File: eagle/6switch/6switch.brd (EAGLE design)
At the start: 100 x 80 mm, 13 parts, among them IC1 MCP23017SP, J1 RELAYBRD, Q1 BC548

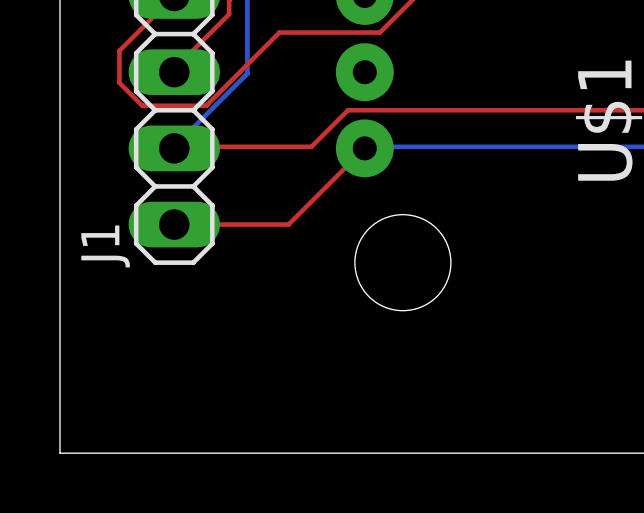
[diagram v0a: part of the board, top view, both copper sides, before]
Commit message: changed some pin names
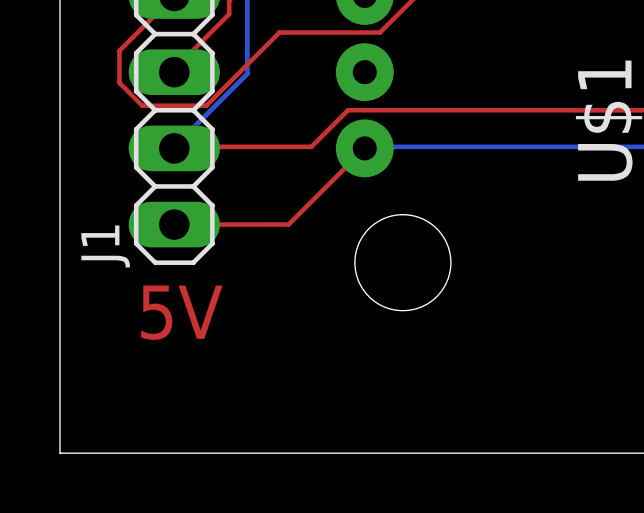
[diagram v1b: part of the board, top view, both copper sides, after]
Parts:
- JP1: value Power -> 5v
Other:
- board text added: "5V"
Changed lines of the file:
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@@
 <wire x1="0" y1="80" x2="0" y2="0" width="0" layer="20"/>
 <text x="3.81" y="68.58" size="1.778" layer="1">https://goo.gl/zYZn5v</text>
-<dimension x1="0" y1="80" x2="43.18" y2="80.01" x3="21.591175" y3="74.931471875" textsize="1.778" layer="1"/>
-<dimension x1="-1.27" y1="0" x2="-1.27" y2="71.12" x3="45.72" y3="35.56" textsize="1.778" layer="1"/>
+<text x="2.54" y="3.81" size="1.778" layer="1">5V</text>
 </plain>
 <attributes>
@@
 </element>
 <element name="U$1" library="ESP12E_DEVKIT" package="ESP12E_DEVKIT" value="ESP12E_DEVKIT" x="21.59" y="27.94"/>
-<element name="JP1" library="jumper" library_urn="urn:adsk.eagle:library:252" package="JP1" package3d_urn="urn:adsk.eagle:package:15455/1" value="Power" x="39.37" y="6.35"/>
+<element name="JP1" library="jumper" library_urn="urn:adsk.eagle:library:252" package="JP1" package3d_urn="urn:adsk.eagle:package:15455/1" value="5v" x="39.37" y="6.35"/>
 <element name="X1" library="con-wago-500" library_urn="urn:adsk.eagle:library:195" package="W237-102" package3d_urn="urn:adsk.eagle:package:10688/1" value="" x="49.53" y="64.77" rot="R90">
 <attribute name="MF" value="" x="49.53" y="64.77" size="1.778" layer="27" rot="R90" display="off"/>

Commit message: eagle board
silkscreen stuff
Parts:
- X1: value (none) -> Sw1
- X2: value (none) -> Sw7
- X3: value (none) -> Sw5
- X4: value (none) -> Sw4
- X5: value (none) -> Sw3
- X6: value (none) -> Sw2
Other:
- board size 100 x 80 mm -> 57.1 x 71.4 mm
- board text added: "1"
- board text added: "2"
- board text added: "3"
- board text added: "4"
- board text added: "4k7"
- board text added: "5"
- board text added: "5v"
- board text added: "6"
- board text added: "BC548"
- board text added: "D0"
- board text added: "Gnd"
- board text added: "Sw1"
- board text added: "Sw2"
- board text added: "Sw3"
- board text added: "Sw4"
- board text added: "Sw5"
- board text added: "Sw6"
- board text added: "USB this end"
- board text added: "Vin"
- board text removed: "5V"

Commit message: dru changed
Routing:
- net N$11: track 78.5 -> 57.0 mm, vias 0 -> 1
- net N$4: track 73.0 -> 90.3 mm
- net N$12: track 71.1 -> 81.5 mm
- net N$9: track 54.6 -> 45.0 mm
- net N$16: track 42.7 -> 33.2 mm
- net N$8: track 69.1 -> 60.5 mm
- net GND: track 179.1 -> 173.3 mm
- net N$14: track 55.9 -> 61.6 mm
- net N$6: track 69.2 -> 63.7 mm
- net N$2: track 34.3 -> 38.6 mm, vias 0 -> 1
- net N$10: track 55.5 -> 52.0 mm
- net N$13: track 74.7 -> 71.6 mm
- net N$15: track 56.8 -> 58.8 mm
- net VCC: track 114.4 -> 112.8 mm
- net N$3: track 42.9 -> 43.5 mm
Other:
- board size 57.1 x 71.4 mm -> 57 x 71.1 mm

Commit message: first board send for production
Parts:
- moved X1 1.96 mm to (48.4, 66.4)
- moved X3 1.96 mm to (48.4, 43.5)
- moved X4 1.96 mm to (48.4, 32.1)
- moved IC1 1.96 mm to (19.2, 62.6)
- moved JP1 1.96 mm to (38.3, 7.98)
- moved J1 1.96 mm to (2.72, 18.1)
- moved X6 1.96 mm to (48.4, 9.25)
- moved Q1 1.96 mm to (39.5, 46.1)
- moved R1 1.96 mm to (38.3, 19.4)
- moved R2 1.96 mm to (38.3, 33.4)
- moved U$1 1.96 mm to (20.5, 29.6)
- moved X2 1.96 mm to (48.4, 55.0)
- moved X5 1.96 mm to (48.4, 20.7)
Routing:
- net N$10: track 52.0 -> 100.8 mm
- net N$12: track 81.5 -> 56.0 mm
- net N$4: track 90.3 -> 68.0 mm, vias 0 -> 1
- net N$13: track 71.6 -> 51.5 mm, vias 0 -> 2
- net N$3: track 43.5 -> 63.2 mm
- net GND: track 173.3 -> 190.1 mm
- net N$14: track 61.6 -> 77.2 mm
- net VCC: track 112.8 -> 125.3 mm, vias 0 -> 1
- net N$6: track 63.7 -> 71.0 mm
- net N$2: track 38.6 -> 34.3 mm, vias 1 -> 0
- net N$11: track 57.0 -> 53.4 mm
- net N$15: track 58.8 -> 61.6 mm
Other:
- board size 57 x 71.1 mm -> 55 x 76.1 mm

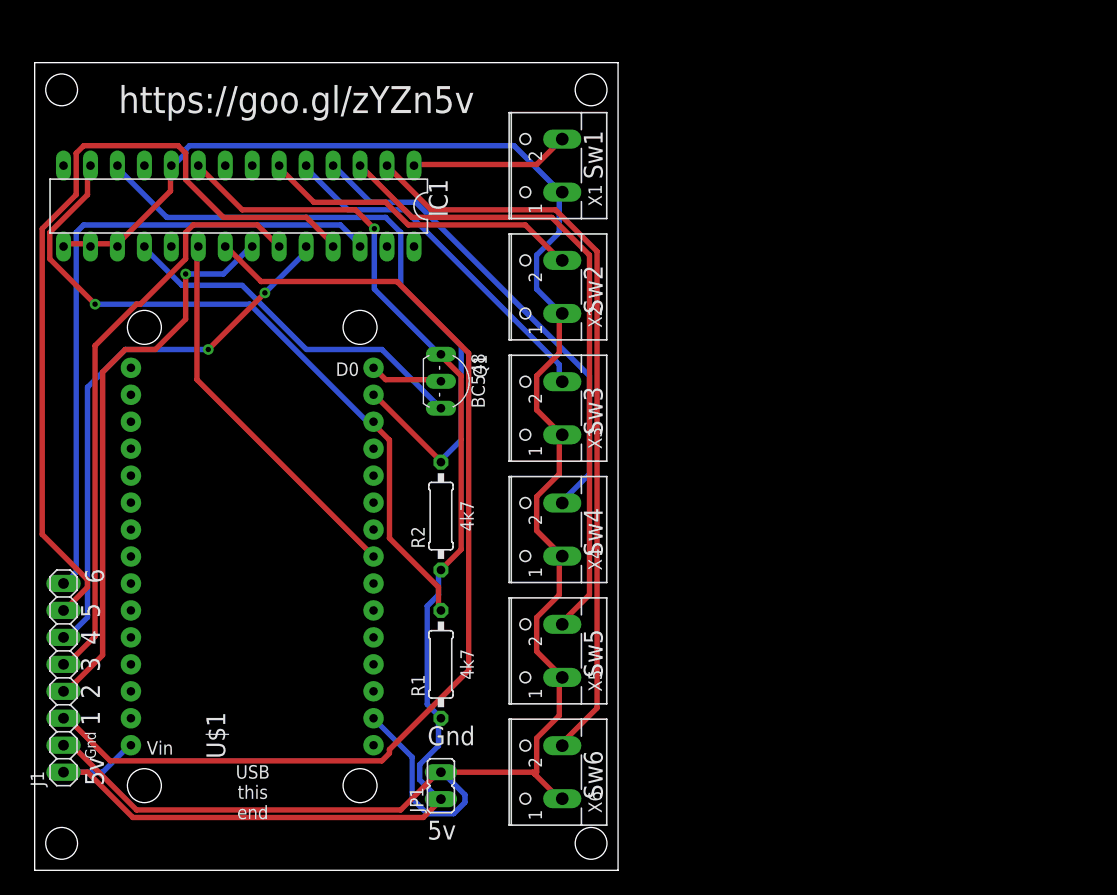
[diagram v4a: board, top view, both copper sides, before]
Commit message: added a 'power down the relay board' tranisistor, more debug, changed types to be more uniform, added a tarpit delay to the web commands, and a minimum time between relays, multiple commands can now be sent on the web api, fixed the NODEMCU size in the board, and the miswired A/B IOs on the MCP
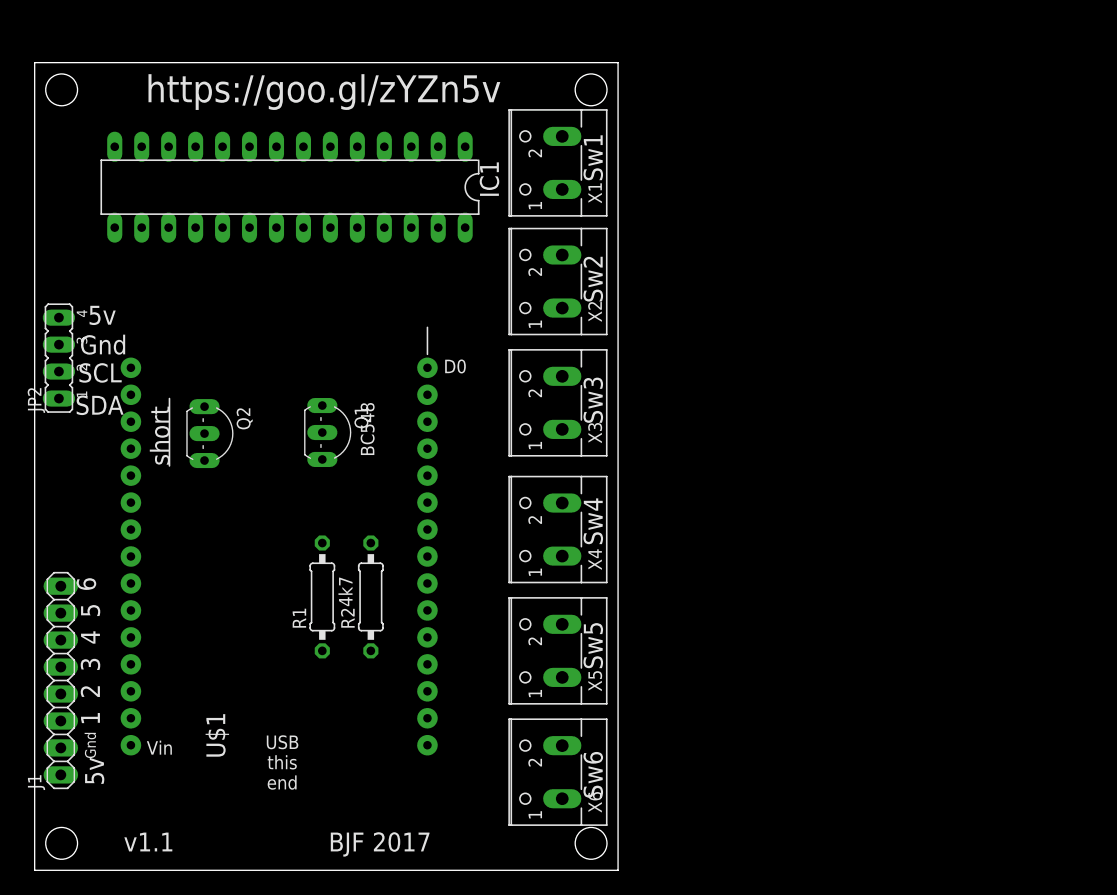
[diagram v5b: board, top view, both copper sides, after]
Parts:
- removed JP1: 5v, jumper:JP1
- added JP2: 5v, jumper:JP4
- added Q2: BC548, transistor-npn:TO92-EBC
- moved R1 12.9 mm to (27.1, 25.8)
- moved Q1 12.2 mm to (28.4, 41.2)
- moved R2 10.1 mm to (31.7, 25.8)
- moved IC1 5.14 mm to (24.1, 64.4)
- moved X2 0.51 mm to (48.4, 55.5)
- moved X3 0.51 mm to (48.4, 44.0)
- moved J1 0.36 mm to (2.46, 17.9)
- moved X1 0.25 mm to (48.4, 66.6)
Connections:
- new net SCL: IC1.12, JP2.2, R2.2, U$1.D1
- new net SDA: IC1.13, JP2.1, R1.2, U$1.D2
- net GND: now also JP2.3; no longer JP1.2
- net N$10: now also X1.2; no longer J1.3
- net N$11: now also IC1.2; no longer IC1.22
- net N$12: now also IC1.3; no longer IC1.23
- net N$13: now also IC1.4; no longer IC1.24
- net N$14: now also IC1.5; no longer IC1.25
- net N$15: now also IC1.6; no longer IC1.26
- net N$16: now also IC1.25; no longer IC1.5
- net N$17: now also IC1.26; no longer IC1.6
- net N$3: now also J1.1, Q2.E; no longer IC1.12, R2.2, U$1.D1
- net N$4: now also Q2.B, U$1.D3; no longer IC1.13, R1.2, U$1.D2
- net N$5: now also IC1.22, X6.2; no longer IC1.1, X1.2
- net N$6: now also IC1.1, J1.3; no longer IC1.2, X6.2
- net N$8: now also IC1.23; no longer IC1.3
- net N$9: now also IC1.24; no longer IC1.4
- net VCC: now also JP2.4, Q2.C; no longer J1.1, JP1.1
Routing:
- net GND: track 190.1 -> 0.00 mm
- net VCC: track 125.3 -> 0.00 mm, vias 1 -> 0
- net N$10: track 100.8 -> 0.00 mm
- net N$14: track 77.2 -> 0.00 mm
- net N$6: track 71.0 -> 0.00 mm
- net N$4: track 68.0 -> 0.00 mm, vias 1 -> 0
- net N$3: track 63.2 -> 0.00 mm
- net N$15: track 61.6 -> 0.00 mm
- net N$8: track 60.9 -> 0.00 mm
- net N$12: track 56.0 -> 0.00 mm
- net N$11: track 53.4 -> 0.00 mm, vias 1 -> 0
- net N$13: track 51.5 -> 0.00 mm, vias 2 -> 0
- net N$9: track 45.4 -> 0.00 mm
- net N$7: track 36.2 -> 0.00 mm
- net N$2: track 34.3 -> 0.00 mm
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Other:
- board text added: "BJF 2017"
- board text added: "SCL"
- board text added: "SDA"
- board text added: "short"
- board text added: "v1.1"
